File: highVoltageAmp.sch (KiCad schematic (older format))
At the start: 18 parts, among them U2 OPA211, U3 OPA211

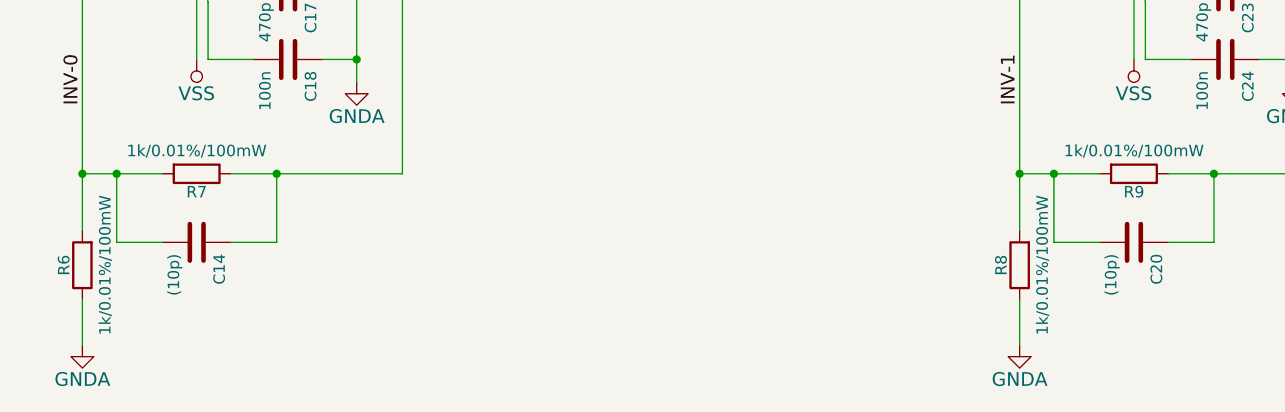
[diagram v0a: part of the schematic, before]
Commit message: Updated all part descriptions
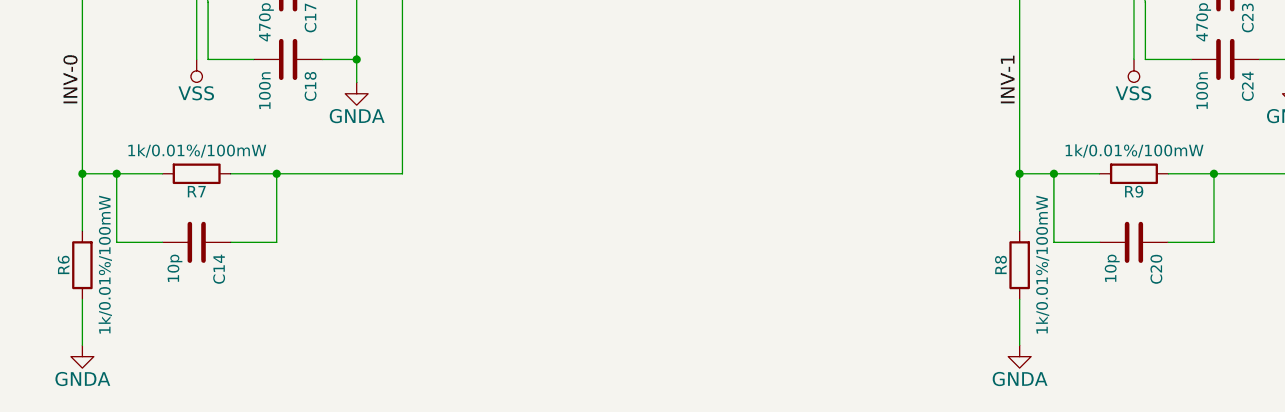
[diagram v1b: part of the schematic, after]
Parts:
- C13, C19: Alt. Order Code (none) -> 77-VJ0603Y103KXACBC; Alt. Supplier (none) -> Mouser; Note (none) -> 10nF/100V X7R 0603 ceramic capacitor; Package (none) -> 0603; Supplier (none) -> Farnell
- C14, C20: value (10p) -> 10p; Alt. Order Code (none) -> 77-VJ0603A100JXACBC; Alt. Supplier (none) -> Mouser; Manufacturer (none) -> Multicomp; Note (none) -> 10pF/50V C0G(NP0) 0603 ceramic capacitor; Order Code (none) -> 2320799; Package (none) -> 0603; Part Number (none) -> MC0603N100J500CT; Supplier (none) -> Farnell
- C15, C18, C21, C24: Alt. Order Code (none) -> 710-885012206095; Alt. Supplier (none) -> Mouser; Package (none) -> 0603; Supplier (none) -> Farnell
- C16, C17, C22, C23: Alt. Order Code (none) -> 710-885012206081; Alt. Supplier (none) -> Mouser; Note (none) -> 470pF/50V C0G(NP0) 0603 ceramic capacitor; Package (none) -> 0603; Supplier (none) -> Farnell
- R6, R7, R8, R9: Alt. Order Code (none) -> 71-PLTT0805Z1001QGT5; Alt. Supplier (none) -> Mouser; Note (none) -> 1kΩ/0.01% 0805 resistor; Package (none) -> 0805; Supplier (none) -> Farnell
- U2, U3: Alt. Order Code (none) -> 595-OPA211AIDGKT; Alt. Supplier (none) -> Mouser; Note (none) -> 1.1-nV/√Hz noise low power precision operational amplifier; Package (none) -> MSOP-8; Supplier (none) -> Farnell

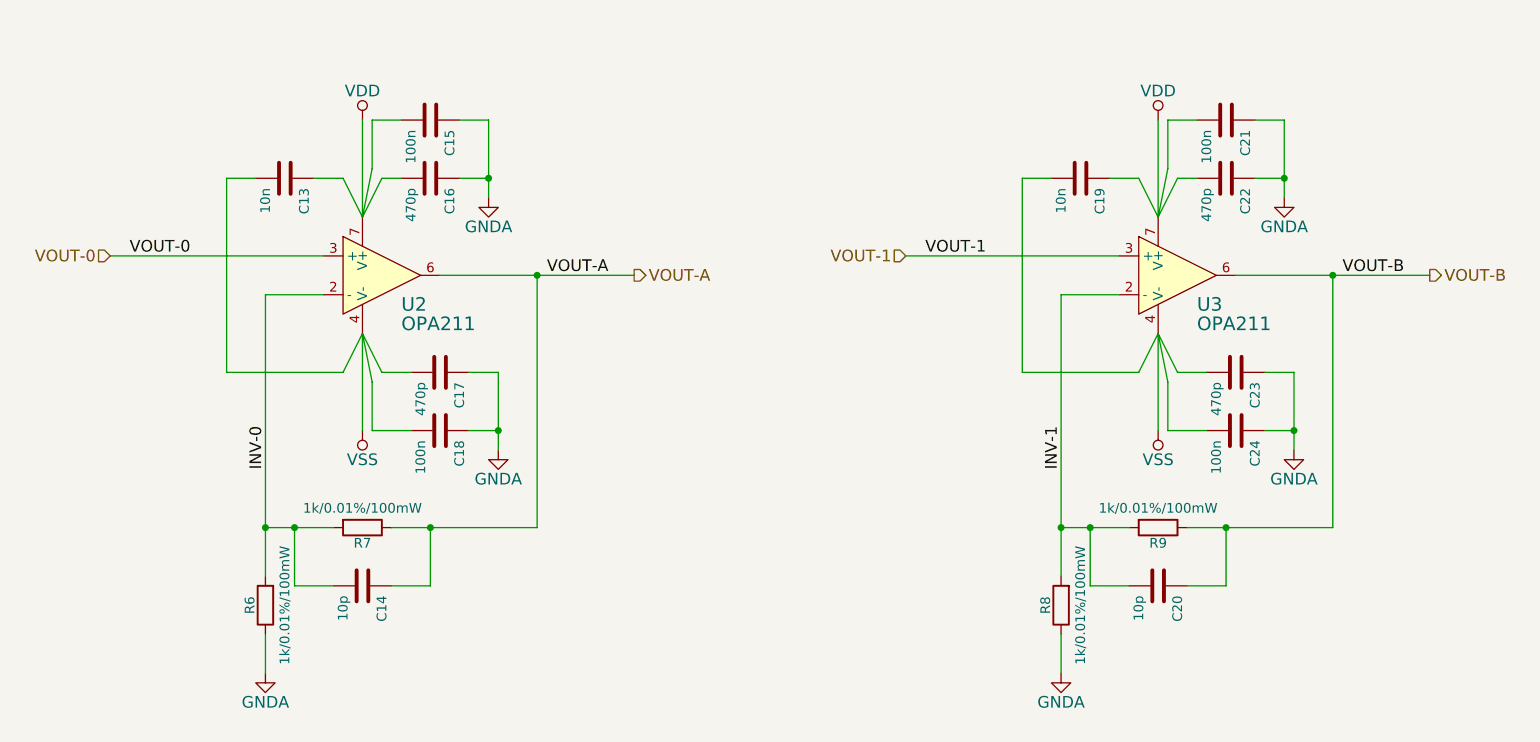
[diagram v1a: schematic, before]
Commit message: Fixed ground problems, added bypass capacitors, added resistor between digital isolator and DAC
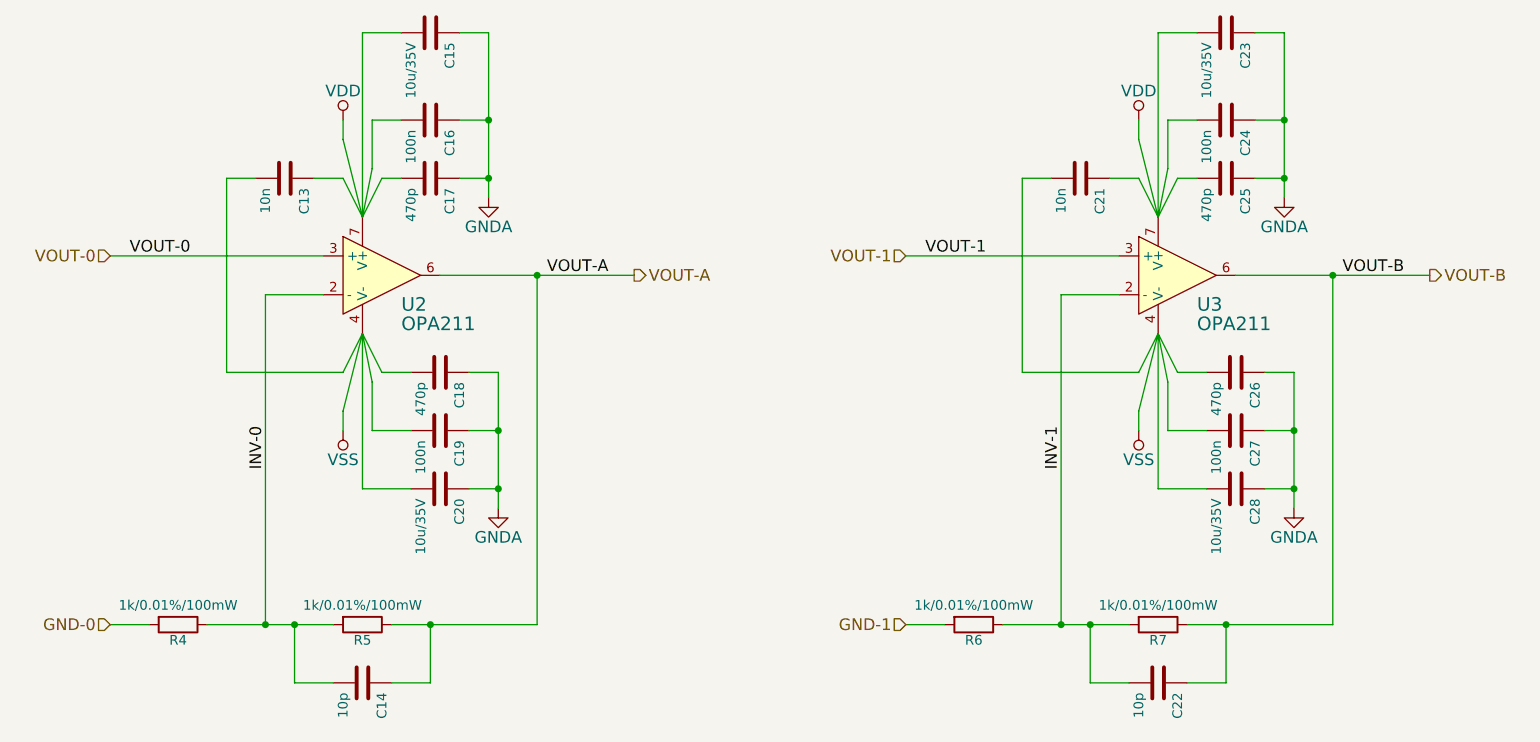
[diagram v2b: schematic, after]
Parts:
- added C15, C20, C23, C28: 10u/35V, Capacitors_SMD:C_1210, symbol C
- renumbered C15 to C16, C16 to C17, C17 to C18, C18 to C19, C19 to C21, C20 to C22, C21 to C24, C22 to C25, C23 to C26, C24 to C27, R6 to R4, R7 to R5, R8 to R6, R9 to R7
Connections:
- net GNDA: now also C15.1, C20.1, C23.1, C28.1; no longer R4.1, R6.1
- net INV-0: now also R4.1; no longer R4.2
- net INV-1: now also R6.1; no longer R6.2
- net VDD: now also C15.2, C23.2
- net VSS: now also C20.2, C28.2
- new net GND-0: R4.2
- new net GND-1: R6.2
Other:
- moved on the sheet: C14, C22, R4, R5, R6, R7

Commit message: Fixed can, 1Ohm resistor descriptions
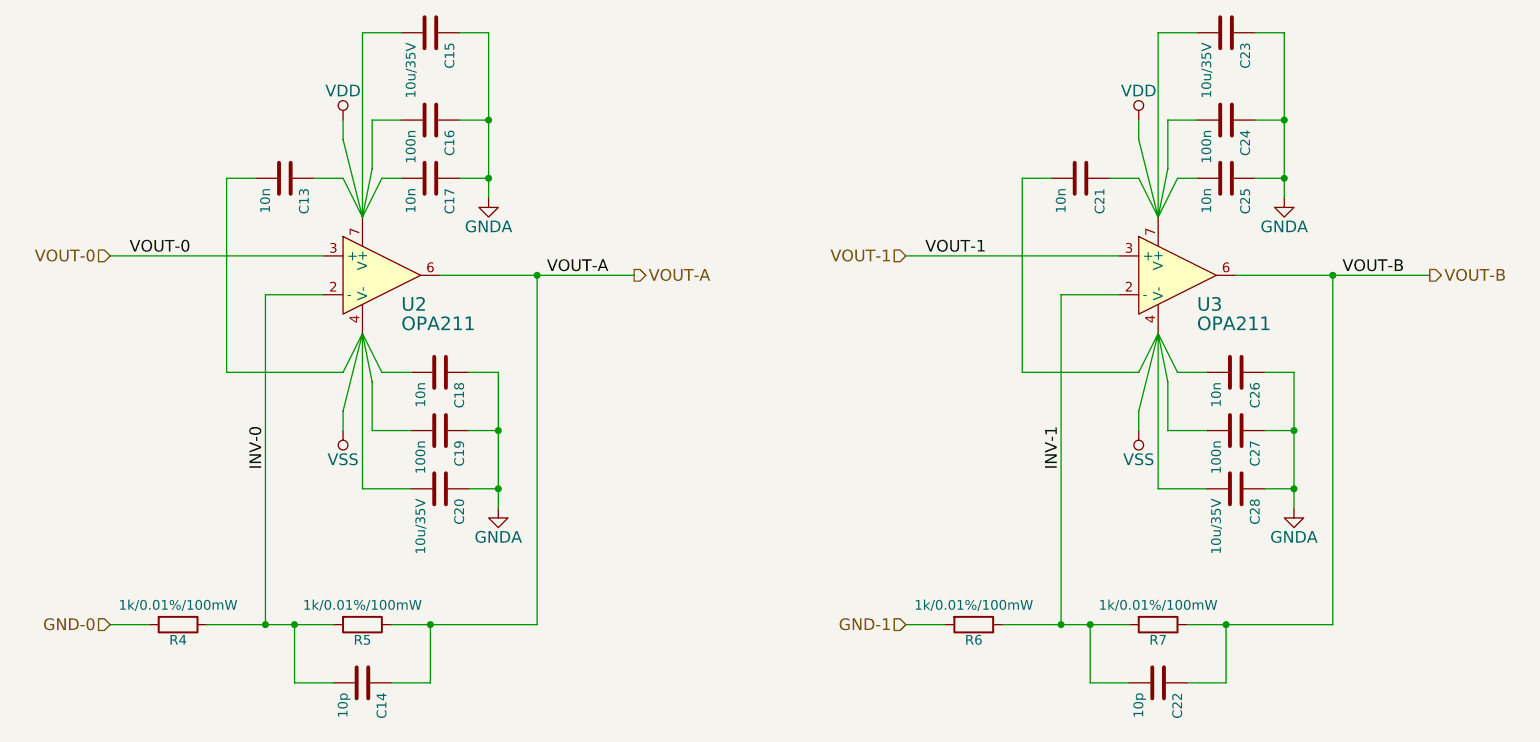
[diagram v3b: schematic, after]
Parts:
- C17, C18, C25, C26: value 470p -> 10n; Alt. Order Code 710-885012206081 -> 77-VJ0603Y103KXACBC; Note 470pF/50V C0G(NP0) 0603 ceramic capacitor -> 10nF/100V X7R 0603 ceramic capacitor; Order Code 1759080 -> 2320786; Part Number MC0603N471J500CT -> MC0603B103K101CT
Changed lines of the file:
@@
 Connection ~ 2950 4500
-$Comp
-L C C17
-U 1 1 55733A19
-P 3650 2200
-F 0 "C17" H 3700 2300 50  0000 L CNN
-F 1 "470p" H 3700 2100 50  0000 L CNN
-F 2 "Capacitors_SMD:C_0603" H 3688 2050 30  0001 C CNN
-F 3 "" H 3650 2200 60  0000 C CNN
-F 4 "MC0603N471J500CT" H 3650 2200 60  0001 C CNN "Part Number"
-F 5 "Multicomp" H 3650 2200 60  0001 C CNN "Manufacturer"
-F 6 "0603" H 3650 2200 60  0001 C CNN "Package"
-F 7 "Farnell" H 3650 2200 60  0001 C CNN "Supplier"
-F 8 "1759080" H 3650 2200 60  0001 C CNN "Order Code"
-F 9 "Mouser" H 3650 2200 60  0001 C CNN "Alt. Supplier"
-F 10 "710-885012206081" H 3650 2200 60  0001 C CNN "Alt. Order Code"
-F 11 "470pF/50V C0G(NP0) 0603 ceramic capacitor" H 3650 2200 60  0001 C CNN "Note"
-	1    3650 2200
-	0    1    1    0
-$EndComp
 $Comp
 L C C16
@@
 	3300 1450 3300 2400
 $Comp
-L VDD #PWR031
+L VDD #PWR034
 U 1 1 55733A28
 P 3200 1900
-F 0 "#PWR031" H 3200 1750 60  0001 C CNN
+F 0 "#PWR034" H 3200 1750 60  0001 C CNN
 F 1 "VDD" H 3200 2050 60  0000 C CNN
 F 2 "" H 3200 1900 60  0000 C CNN
@@
 $EndComp
 $Comp
-L VSS #PWR032
+L VSS #PWR035
 U 1 1 55733A2E
 P 3200 3500
-F 0 "#PWR032" H 3200 3350 60  0001 C CNN
+F 0 "#PWR035" H 3200 3350 60  0001 C CNN
 F 1 "VSS" H 3200 3650 60  0000 C CNN
 F 2 "" H 3200 3500 60  0000 C CNN
@@
 P 3700 3200
 F 0 "C18" H 3750 3300 50  0000 L CNN
-F 1 "470p" H 3750 3100 50  0000 L CNN
+F 1 "10n" H 3750 3100 50  0000 L CNN
 F 2 "Capacitors_SMD:C_0603" H 3738 3050 30  0001 C CNN
 F 3 "" H 3700 3200 60  0000 C CNN
-F 4 "MC0603N471J500CT" H 3700 3200 60  0001 C CNN "Part Number"
+F 4 "MC0603B103K101CT" H 3700 3200 60  0001 C CNN "Part Number"
 F 5 "Multicomp" H 3700 3200 60  0001 C CNN "Manufacturer"
 F 6 "0603" H 3700 3200 60  0001 C CNN "Package"
 F 7 "Farnell" H 3700 3200 60  0001 C CNN "Supplier"
-F 8 "1759080" H 3700 3200 60  0001 C CNN "Order Code"
+F 8 "2320786" H 3700 3200 60  0001 C CNN "Order Code"
 F 9 "Mouser" H 3700 3200 60  0001 C CNN "Alt. Supplier"
-F 10 "710-885012206081" H 3700 3200 60  0001 C CNN "Alt. Order Code"
-F 11 "470pF/50V C0G(NP0) 0603 ceramic capacitor" H 3700 3200 60  0001 C CNN "Note"
+F 10 "77-VJ0603Y103KXACBC" H 3700 3200 60  0001 C CNN "Alt. Order Code"
+F 11 "10nF/100V X7R 0603 ceramic capacitor" H 3700 3200 60  0001 C CNN "Note"
 	1    3700 3200
 	0    1    1    0
@@
 Connection ~ 3950 2200
 $Comp
-L GNDA #PWR033
+L GNDA #PWR036
 U 1 1 55733A60
 P 3950 2300
-F 0 "#PWR033" H 3950 2050 60  0001 C CNN
+F 0 "#PWR036" H 3950 2050 60  0001 C CNN
 F 1 "GNDA" H 3950 2150 60  0000 C CNN
 F 2 "" H 3950 2300 60  0000 C CNN
@@
 $EndComp
 $Comp
-L GNDA #PWR034
+L GNDA #PWR037
 U 1 1 55733A66
 P 4000 3900
-F 0 "#PWR034" H 4000 3650 60  0001 C CNN
+F 0 "#PWR037" H 4000 3650 60  0001 C CNN
 F 1 "GNDA" H 4000 3750 60  0000 C CNN
 F 2 "" H 4000 3900 60  0000 C CNN
@@
 Connection ~ 7050 4500
 $Comp
-L C C25
-U 1 1 5573425E
-P 7750 2200
-F 0 "C25" H 7800 2300 50  0000 L CNN
-F 1 "470p" H 7800 2100 50  0000 L CNN
-F 2 "Capacitors_SMD:C_0603" H 7788 2050 30  0001 C CNN
-F 3 "" H 7750 2200 60  0000 C CNN
-F 4 "MC0603N471J500CT" H 7750 2200 60  0001 C CNN "Part Number"
-F 5 "Multicomp" H 7750 2200 60  0001 C CNN "Manufacturer"
-F 6 "0603" H 7750 2200 60  0001 C CNN "Package"
-F 7 "Farnell" H 7750 2200 60  0001 C CNN "Supplier"
-F 8 "1759080" H 7750 2200 60  0001 C CNN "Order Code"
-F 9 "Mouser" H 7750 2200 60  0001 C CNN "Alt. Supplier"
-F 10 "710-885012206081" H 7750 2200 60  0001 C CNN "Alt. Order Code"
-F 11 "470pF/50V C0G(NP0) 0603 ceramic capacitor" H 7750 2200 60  0001 C CNN "Note"
-	1    7750 2200
-	0    1    1    0
-$EndComp
-$Comp
 L C C24
 U 1 1 55734264
@@
 $EndComp
 $Comp
-L C C26
-U 1 1 5573428A
-P 7800 3200
-F 0 "C26" H 7850 3300 50  0000 L CNN
-F 1 "470p" H 7850 3100 50  0000 L CNN
-F 2 "Capacitors_SMD:C_0603" H 7838 3050 30  0001 C CNN
-F 3 "" H 7800 3200 60  0000 C CNN
-F 4 "MC0603N471J500CT" H 7800 3200 60  0001 C CNN "Part Number"
-F 5 "Multicomp" H 7800 3200 60  0001 C CNN "Manufacturer"
-F 6 "0603" H 7800 3200 60  0001 C CNN "Package"
-F 7 "Farnell" H 7800 3200 60  0001 C CNN "Supplier"
-F 8 "1759080" H 7800 3200 60  0001 C CNN "Order Code"
-F 9 "Mouser" H 7800 3200 60  0001 C CNN "Alt. Supplier"
-F 10 "710-885012206081" H 7800 3200 60  0001 C CNN "Alt. Order Code"
-F 11 "470pF/50V C0G(NP0) 0603 ceramic capacitor" H 7800 3200 60  0001 C CNN "Note"
-	1    7800 3200
-	0    1    1    0
-$EndComp
-$Comp
 L C C27
 U 1 1 55734290
@@
 Connection ~ 8050 2200
 $Comp
-L GNDA #PWR035
+L GNDA #PWR038
 U 1 1 557342A0
 P 8050 2300
-F 0 "#PWR035" H 8050 2050 60  0001 C CNN
+F 0 "#PWR038" H 8050 2050 60  0001 C CNN
 F 1 "GNDA" H 8050 2150 60  0000 C CNN
 F 2 "" H 8050 2300 60  0000 C CNN
@@
 $EndComp
 $Comp
-L GNDA #PWR036
+L GNDA #PWR039
 U 1 1 55742E56
 P 8100 3900
-F 0 "#PWR036" H 8100 3650 60  0001 C CNN
+F 0 "#PWR039" H 8100 3650 60  0001 C CNN
 F 1 "GNDA" H 8100 3750 60  0000 C CNN
 F 2 "" H 8100 3900 60  0000 C CNN
@@
 	7400 1450 7400 2400
 $Comp
-L VDD #PWR037
+L VDD #PWR040
 U 1 1 56DFC4D3
 P 7300 1900
-F 0 "#PWR037" H 7300 1750 60  0001 C CNN
+F 0 "#PWR040" H 7300 1750 60  0001 C CNN
 F 1 "VDD" H 7300 2050 60  0000 C CNN
 F 2 "" H 7300 1900 60  0000 C CNN
@@
 $EndComp
 $Comp
-L VSS #PWR038
+L VSS #PWR041
 U 1 1 56DFC6F8
 P 7300 3500
-F 0 "#PWR038" H 7300 3350 60  0001 C CNN
+F 0 "#PWR041" H 7300 3350 60  0001 C CNN
 F 1 "VSS" H 7300 3650 60  0000 C CNN
 F 2 "" H 7300 3500 60  0000 C CNN
@@
 Text HLabel 6100 4500 0    60   Input ~ 0
 GND-1
+$Comp
+L C C17
+U 1 1 56F1485B
+P 3650 2200
+F 0 "C17" H 3700 2300 50  0000 L CNN
+F 1 "10n" H 3700 2100 50  0000 L CNN
+F 2 "Capacitors_SMD:C_0603" H 3688 2050 30  0001 C CNN
+F 3 "" H 3650 2200 60  0000 C CNN
+F 4 "MC0603B103K101CT" H 3650 2200 60  0001 C CNN "Part Number"
+F 5 "Multicomp" H 3650 2200 60  0001 C CNN "Manufacturer"
+F 6 "0603" H 3650 2200 60  0001 C CNN "Package"
+F 7 "Farnell" H 3650 2200 60  0001 C CNN "Supplier"
+F 8 "2320786" H 3650 2200 60  0001 C CNN "Order Code"
+F 9 "Mouser" H 3650 2200 60  0001 C CNN "Alt. Supplier"
+F 10 "77-VJ0603Y103KXACBC" H 3650 2200 60  0001 C CNN "Alt. Order Code"
+F 11 "10nF/100V X7R 0603 ceramic capacitor" H 3650 2200 60  0001 C CNN "Note"
+	1    3650 2200
+	0    1    1    0
+$EndComp
+$Comp
+L C C25
+U 1 1 56F1493C
+P 7750 2200
+F 0 "C25" H 7800 2300 50  0000 L CNN
+F 1 "10n" H 7800 2100 50  0000 L CNN
+F 2 "Capacitors_SMD:C_0603" H 7788 2050 30  0001 C CNN
+F 3 "" H 7750 2200 60  0000 C CNN
+F 4 "MC0603B103K101CT" H 7750 2200 60  0001 C CNN "Part Number"
+F 5 "Multicomp" H 7750 2200 60  0001 C CNN "Manufacturer"
+F 6 "0603" H 7750 2200 60  0001 C CNN "Package"
+F 7 "Farnell" H 7750 2200 60  0001 C CNN "Supplier"
+F 8 "2320786" H 7750 2200 60  0001 C CNN "Order Code"
+F 9 "Mouser" H 7750 2200 60  0001 C CNN "Alt. Supplier"
+F 10 "77-VJ0603Y103KXACBC" H 7750 2200 60  0001 C CNN "Alt. Order Code"
+F 11 "10nF/100V X7R 0603 ceramic capacitor" H 7750 2200 60  0001 C CNN "Note"
+	1    7750 2200
+	0    1    1    0
+$EndComp
+$Comp
+L C C26
+U 1 1 56F14B0C
+P 7800 3200
+F 0 "C26" H 7850 3300 50  0000 L CNN
+F 1 "10n" H 7850 3100 50  0000 L CNN
+F 2 "Capacitors_SMD:C_0603" H 7838 3050 30  0001 C CNN
+F 3 "" H 7800 3200 60  0000 C CNN
+F 4 "MC0603B103K101CT" H 7800 3200 60  0001 C CNN "Part Number"
+F 5 "Multicomp" H 7800 3200 60  0001 C CNN "Manufacturer"
+F 6 "0603" H 7800 3200 60  0001 C CNN "Package"
+F 7 "Farnell" H 7800 3200 60  0001 C CNN "Supplier"
+F 8 "2320786" H 7800 3200 60  0001 C CNN "Order Code"
+F 9 "Mouser" H 7800 3200 60  0001 C CNN "Alt. Supplier"
+F 10 "77-VJ0603Y103KXACBC" H 7800 3200 60  0001 C CNN "Alt. Order Code"
+F 11 "10nF/100V X7R 0603 ceramic capacitor" H 7800 3200 60  0001 C CNN "Note"
+	1    7800 3200
+	0    1    1    0
+$EndComp
 $EndSCHEMATC

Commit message: Finalized PCB for production
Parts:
- C13, C17, C18, C21, C25, C26: Alt. Order Code 77-VJ0603Y103KXACBC -> 603-CC603KRX7R9BB103; Manufacturer Multicomp -> Yageo; Note 10nF/100V X7R 0603 ceramic capacitor -> 10nF/50V X7R 0603 ceramic capacitor; Order Code 2320786 -> 722236; Part Number MC0603B103K101CT -> CC0603KRX7R9BB103
- C14, C22: Alt. Order Code 77-VJ0603A100JXACBC -> 603-C0603JRNPO9BN100; Manufacturer Multicomp -> Yageo; Order Code 2320799 -> 721967; Part Number MC0603N100J500CT -> CC0603JRNPO9BN100
- C16, C19, C24, C27: Alt. Order Code 710-885012206095 -> 603-CC603KRX7R9BB104; Manufacturer Multicomp -> Yageo; Note (none) -> 100nF/50V X7R 0603 ceramic capacitor; Order Code 1759122 -> 1362556; Part Number MC0603B104K500CT -> CC0603KRX7R9BB104
